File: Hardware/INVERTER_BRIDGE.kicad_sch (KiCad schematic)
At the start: 69 parts, among them Q1 CSD19532Q5B, Q2 CSD19532Q5B, Q3 CSD19532Q5B, Q4 CSD19532Q5B, Q5 CSD19532Q5B, Q6 CSD19532Q5B, U12 UCC27282DRCR, U13 INA240A1PWR, U14 UCC27282DRCR, U15 INA240A1PWR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

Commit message: 拉线，删除电荷泵，修改10Vdcdc斜坡补偿
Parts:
- removed D15, D18, D21: 11V,350mW, Diode_SMD:D_SOD-123, symbol HPM6280Foc:BZT52C11
- removed R27, R32, R37: 10K,1%, Resistor_SMD:R_0402_1005Metric, symbol HPM6280Foc:0402WGF1002TCE

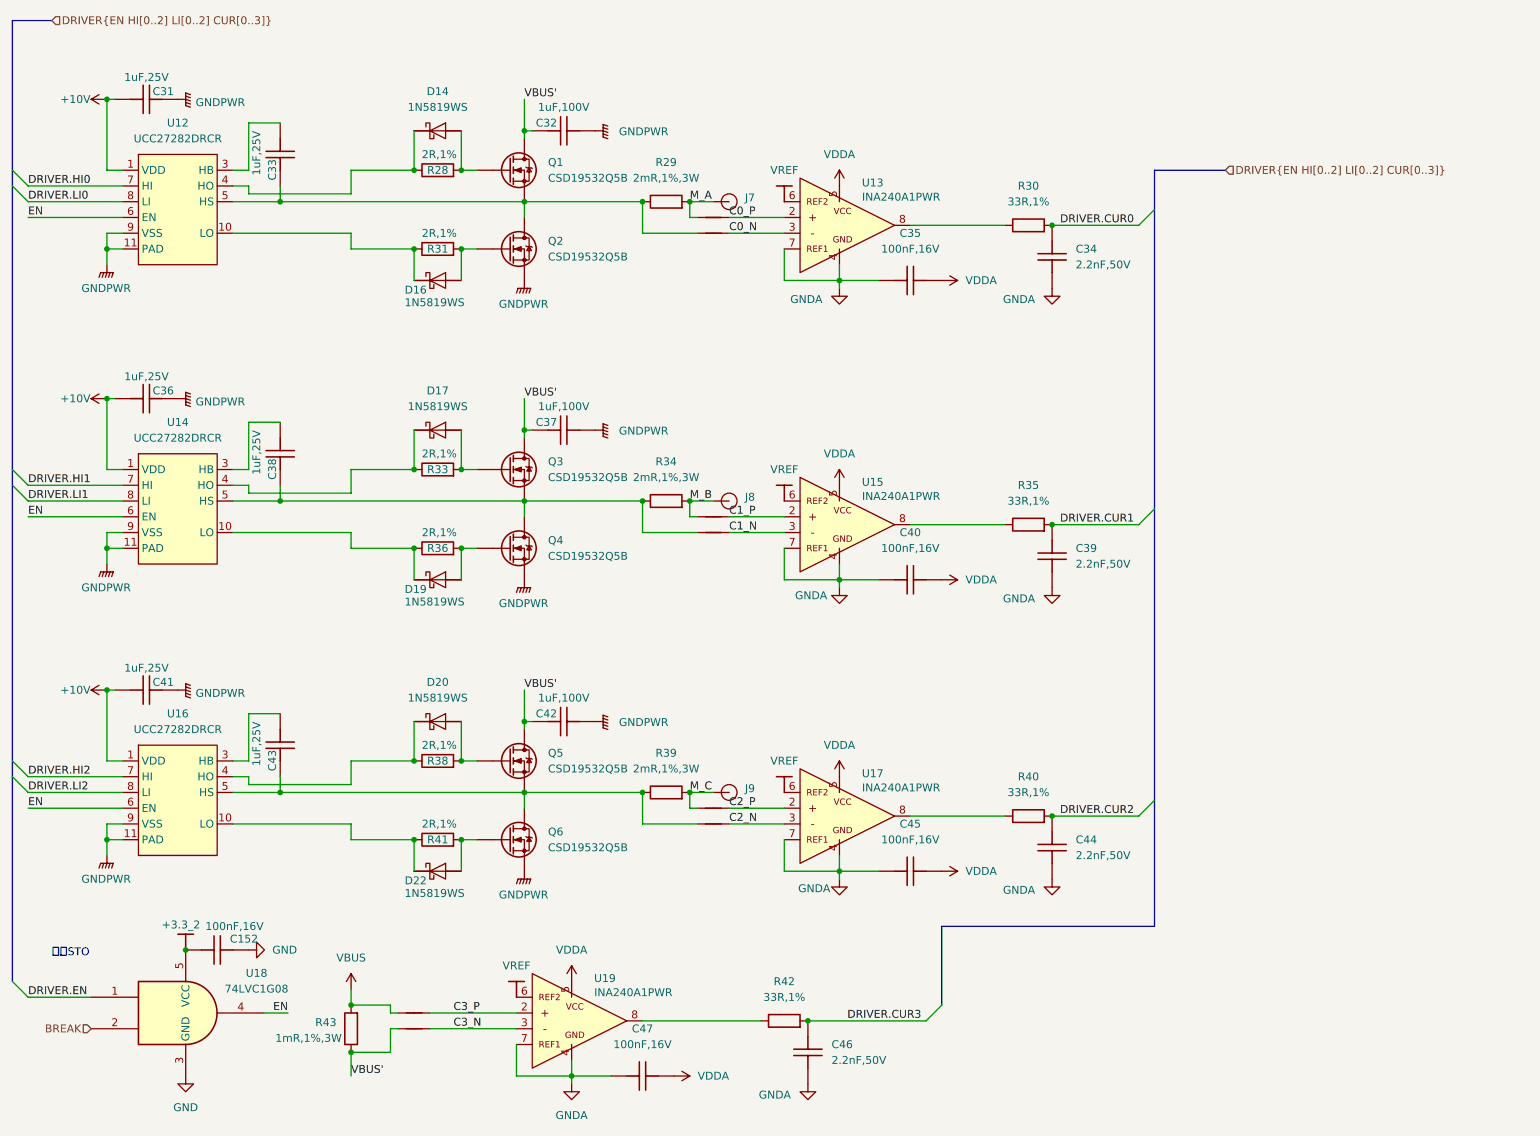
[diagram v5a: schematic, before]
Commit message: PCB和foc_demo
PCB：
部分信号增加测试点
半桥增加栅极电容和RC吸收（待定），泄放mos是否需要栅极电容待测
软件：
增加foc_demo半成品
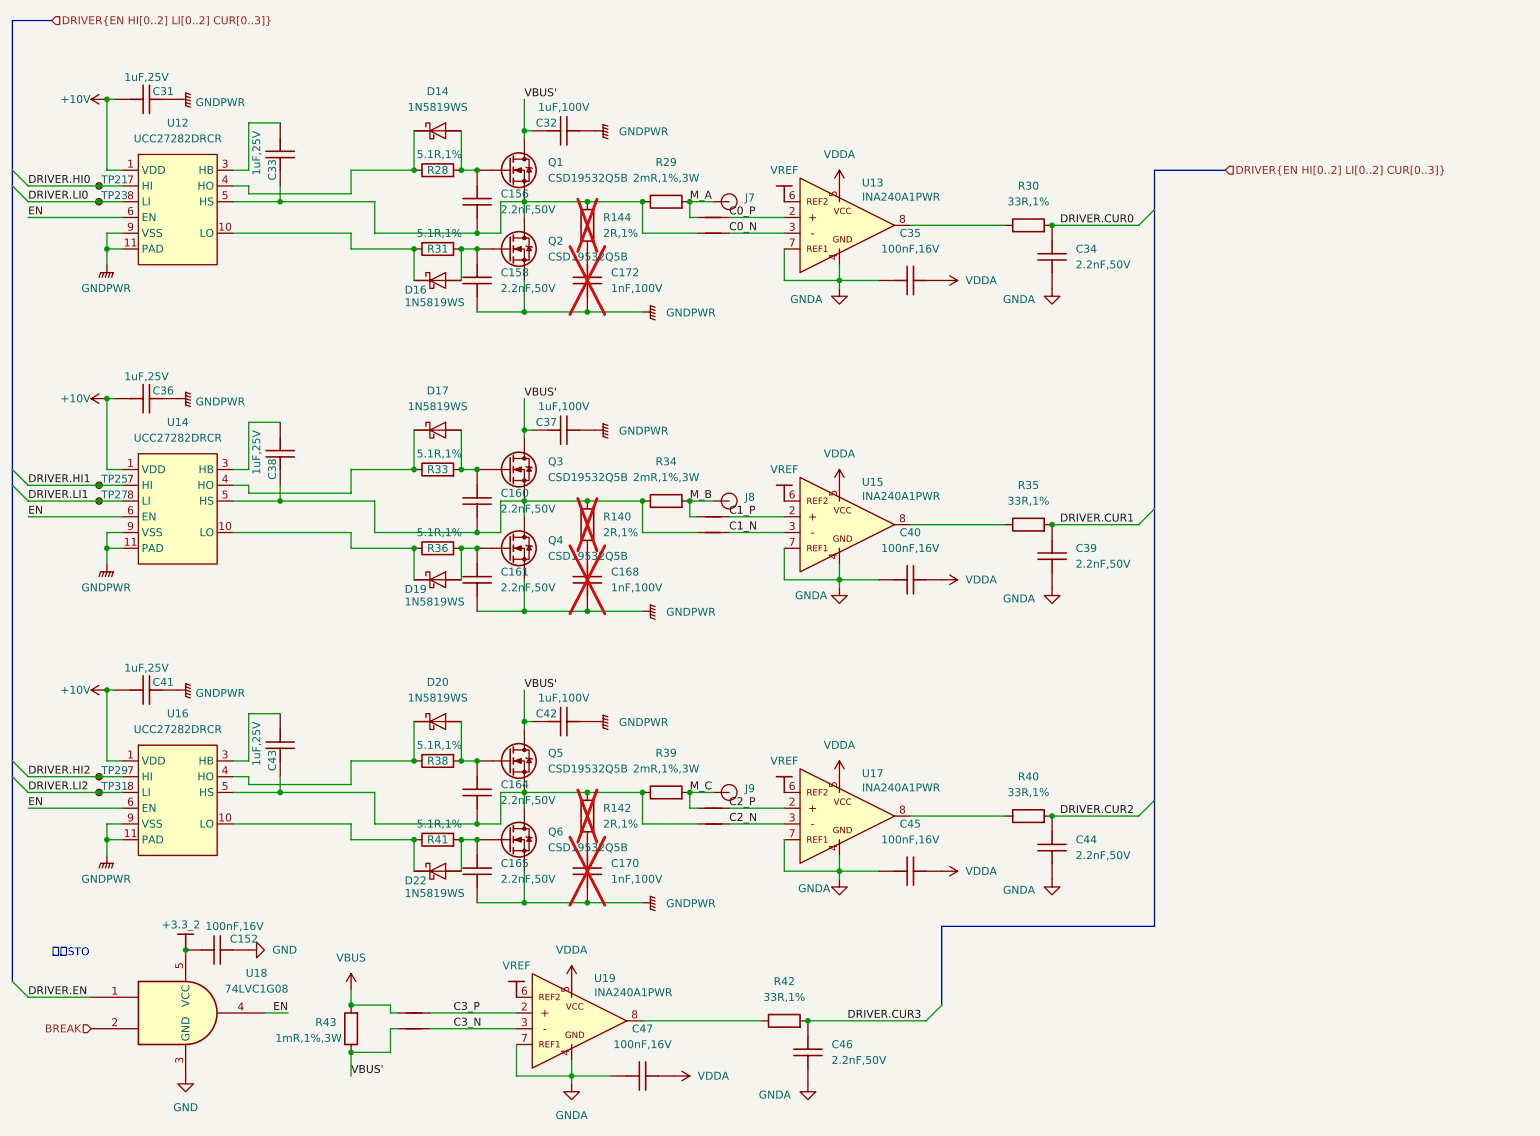
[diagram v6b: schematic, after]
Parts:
- added C156, C158, C160, C161, C164, C165: 2.2nF,50V, Capacitor_SMD:C_0402_1005Metric, symbol HPM6280Foc:0402B222K500NT
- added C168, C170, C172: 1nF,100V, Capacitor_SMD:C_0402_1005Metric, symbol HPM6280Foc:CC0402KRX7R0BB102
- added R140, R142, R144: 2R,1%, Resistor_SMD:R_0402_1005Metric, symbol HPM6280Foc:0402WGF200KTCE
- added TP21, TP23, TP25, TP27, TP29, TP31: ~, Library:test_point_0.5mm, symbol HPM6280Foc:test_point
- R28, R31, R33, R36, R38, R41: value 2R,1% -> 5.1R,1%; symbol HPM6280Foc:0402WGF200KTCE -> HPM6280Foc:0402WGF510KTCE; 立创编号 C270630 -> C25128
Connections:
- net DRIVER.HI0: now also TP21.1
- net DRIVER.HI1: now also TP25.1
- net DRIVER.HI2: now also TP29.1
- net DRIVER.LI0: now also TP23.1
- net DRIVER.LI1: now also TP27.1
- net DRIVER.LI2: now also TP31.1
- net GNDPWR: now also C158.2, C161.2, C165.2, C168.2, C170.2, C172.2
- net at D17.2 (A), Q3.2 (G), R33.2: now also C160.1
- net at C43.2, NT6.1, Q5.3 (S)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: now also C164.2, R142.2
- net at D22.2 (A), Q6.2 (G), R41.2: now also C165.1
- net at D19.2 (A), Q4.2 (G), R36.2: now also C161.1
- net at D14.2 (A), Q1.2 (G), R28.2: now also C156.1
- net at C38.2, NT4.1, Q3.3 (S)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: now also C160.2, R140.2
- net at D20.2 (A), Q5.2 (G), R38.2: now also C164.1
- net at C33.2, NT2.1, Q1.3 (S)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: now also C156.2, R144.2
- net at D16.2 (A), Q2.2 (G), R31.2: now also C158.1
- new net: C168.1, R140.1
- new net: C170.1, R142.1
- new net: C172.1, R144.1

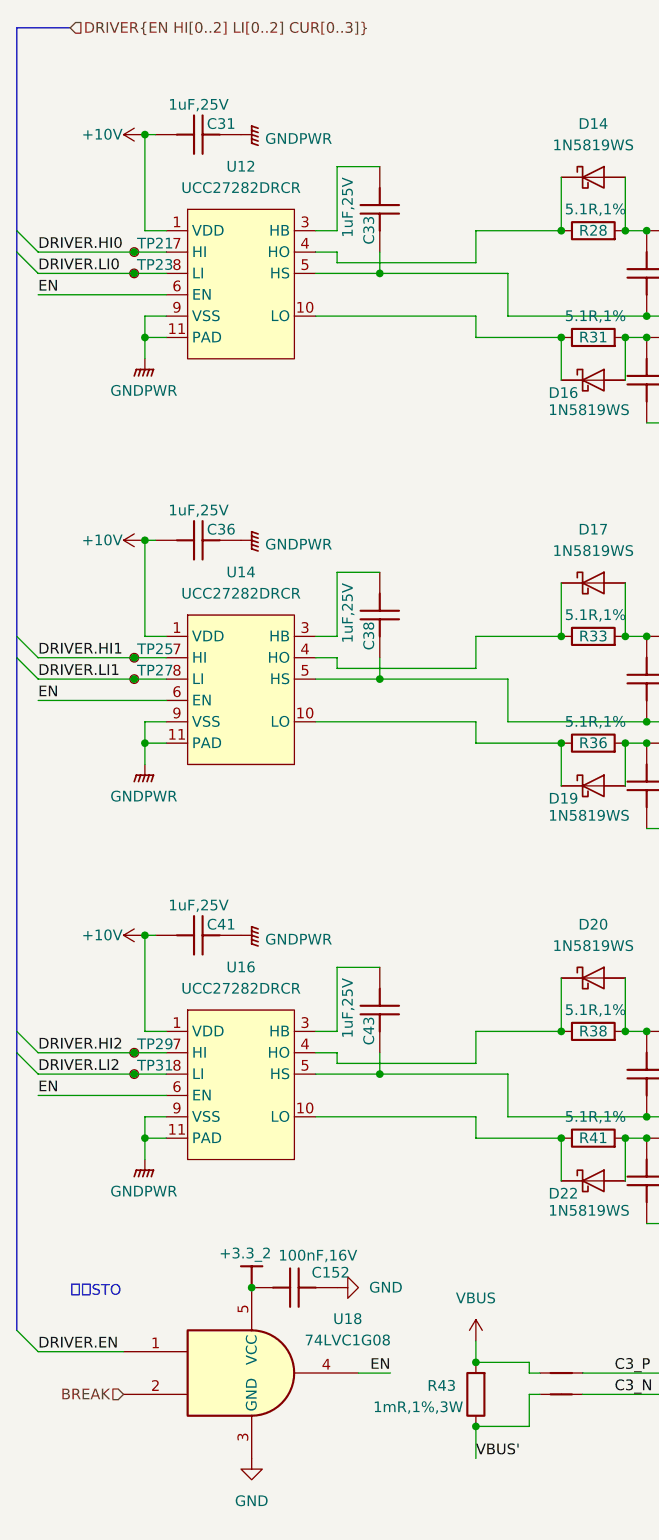
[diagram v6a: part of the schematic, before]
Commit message: PCB优化，修改母线电流采样电阻为2mR，栅极驱动器输入pwm增加滤波防干扰，其他少量优化
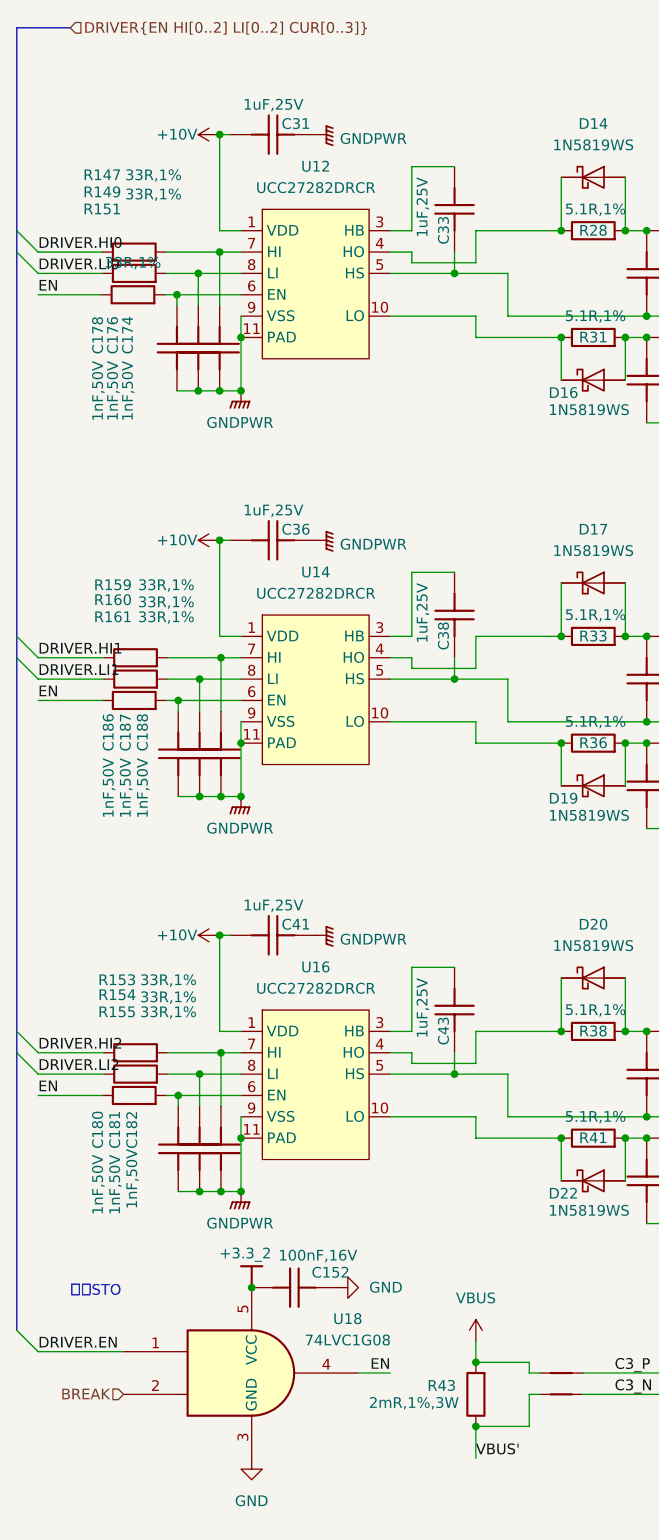
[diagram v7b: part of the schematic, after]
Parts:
- removed TP21, TP23, TP25, TP27, TP29, TP31: ~, Library:test_point_0.5mm, symbol HPM6280Foc:test_point
- added C174, C176, C178, C180, C181, C182, C186, C187, C188: 1nF,50V, Capacitor_SMD:C_0201_0603Metric, symbol HPM6280Foc:CC0201KRX7R9BB102
- added R147, R149, R151, R153, R154, R155, R159, R160, R161: 33R,1%, Resistor_SMD:R_0201_0603Metric, symbol HPM6280Foc:RC0201FR-0733RL
- R43: value 1mR,1%,3W -> 2mR,1%,3W; symbol HPM6280Foc:HoJLR2512-3W-1mR-1% -> HPM6280Foc:HoLLR2512-3W-2mR-1%; 华秋编号 G6676410 -> G11502563; 立创编号 C2903470 -> C2994640
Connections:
- net DRIVER.HI0: now also R147.1; no longer U12.7 (HI)
- net DRIVER.HI1: now also R159.1; no longer U14.7 (HI)
- net DRIVER.HI2: now also R153.1; no longer U16.7 (HI)
- net DRIVER.LI0: now also R149.1; no longer U12.8 (LI)
- net DRIVER.LI1: now also R160.1; no longer U14.8 (LI)
- net DRIVER.LI2: now also R154.1; no longer U16.8 (LI)
- net EN: now also R151.1, R155.1, R161.1; no longer U12.6 (EN), U14.6 (EN), U16.6 (EN)
- net GNDPWR: now also C174.2, C176.2, C178.2, C180.2, C181.2, C182.2, C186.2, C187.2, C188.2
- new net: C181.1, R154.2, U16.8 (LI)
- new net: C188.1, R159.2, U14.7 (HI)
- new net: C187.1, R160.2, U14.8 (LI)
- new net: C182.1, R153.2, U16.7 (HI)
- new net: C174.1, R147.2, U12.7 (HI)
- new net: C176.1, R149.2, U12.8 (LI)
- new net: C186.1, R161.2, U14.6 (EN)
- new net: C180.1, R155.2, U16.6 (EN)
- new net: C178.1, R151.2, U12.6 (EN)
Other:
- moved on the sheet: C31, C33, C36, C38, C41, C43, U12, U14, U16

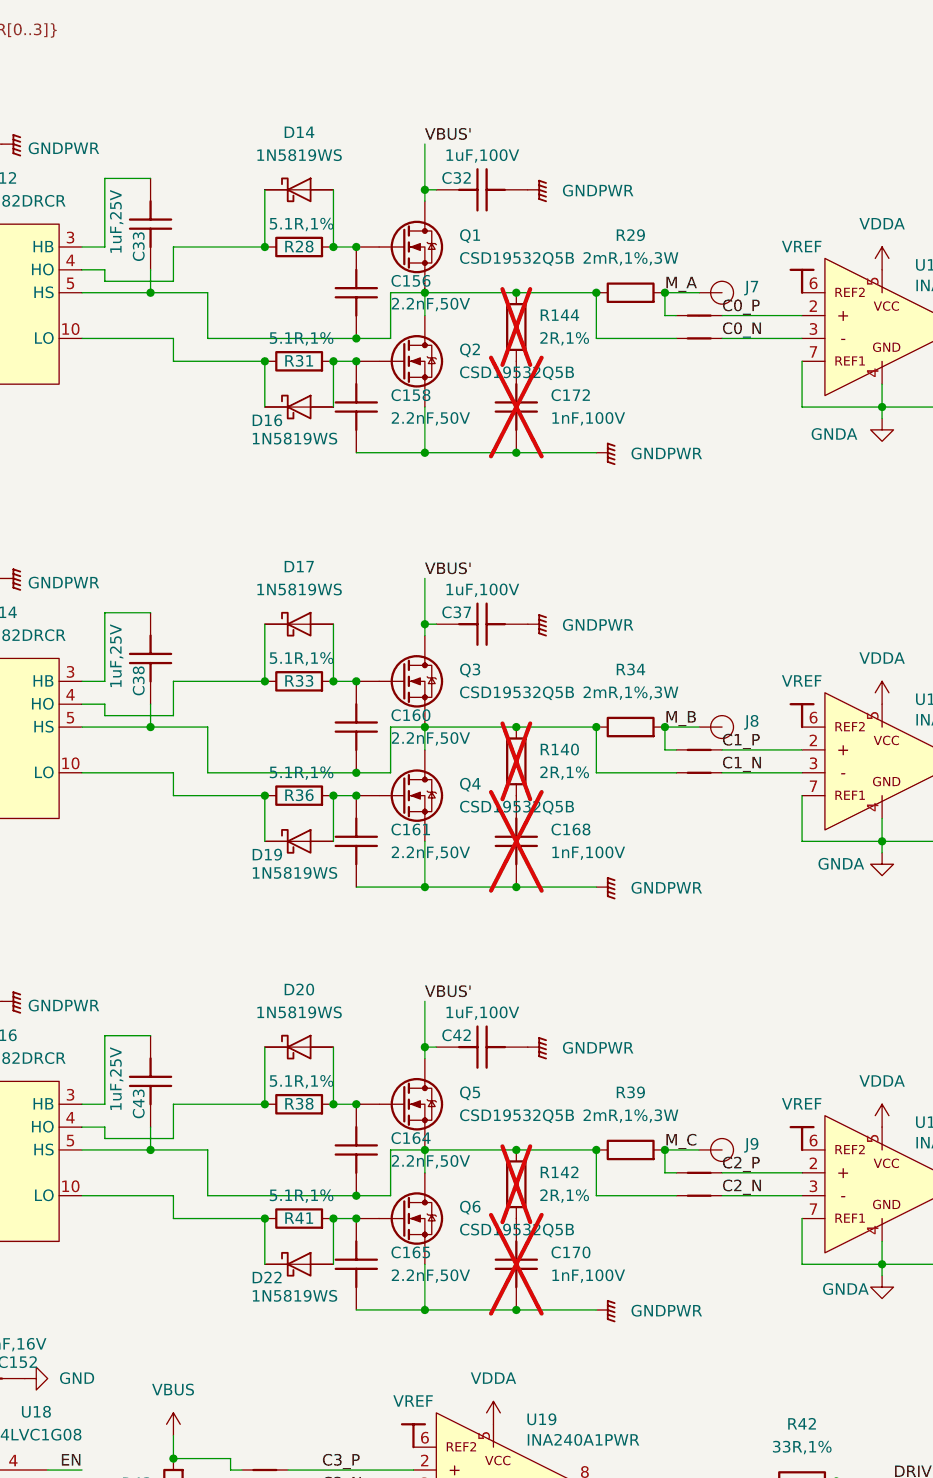
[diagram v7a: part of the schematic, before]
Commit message: PCB修改栅极电阻，增加上侧RC吸收电路，同步修改软件死区时间到150ns
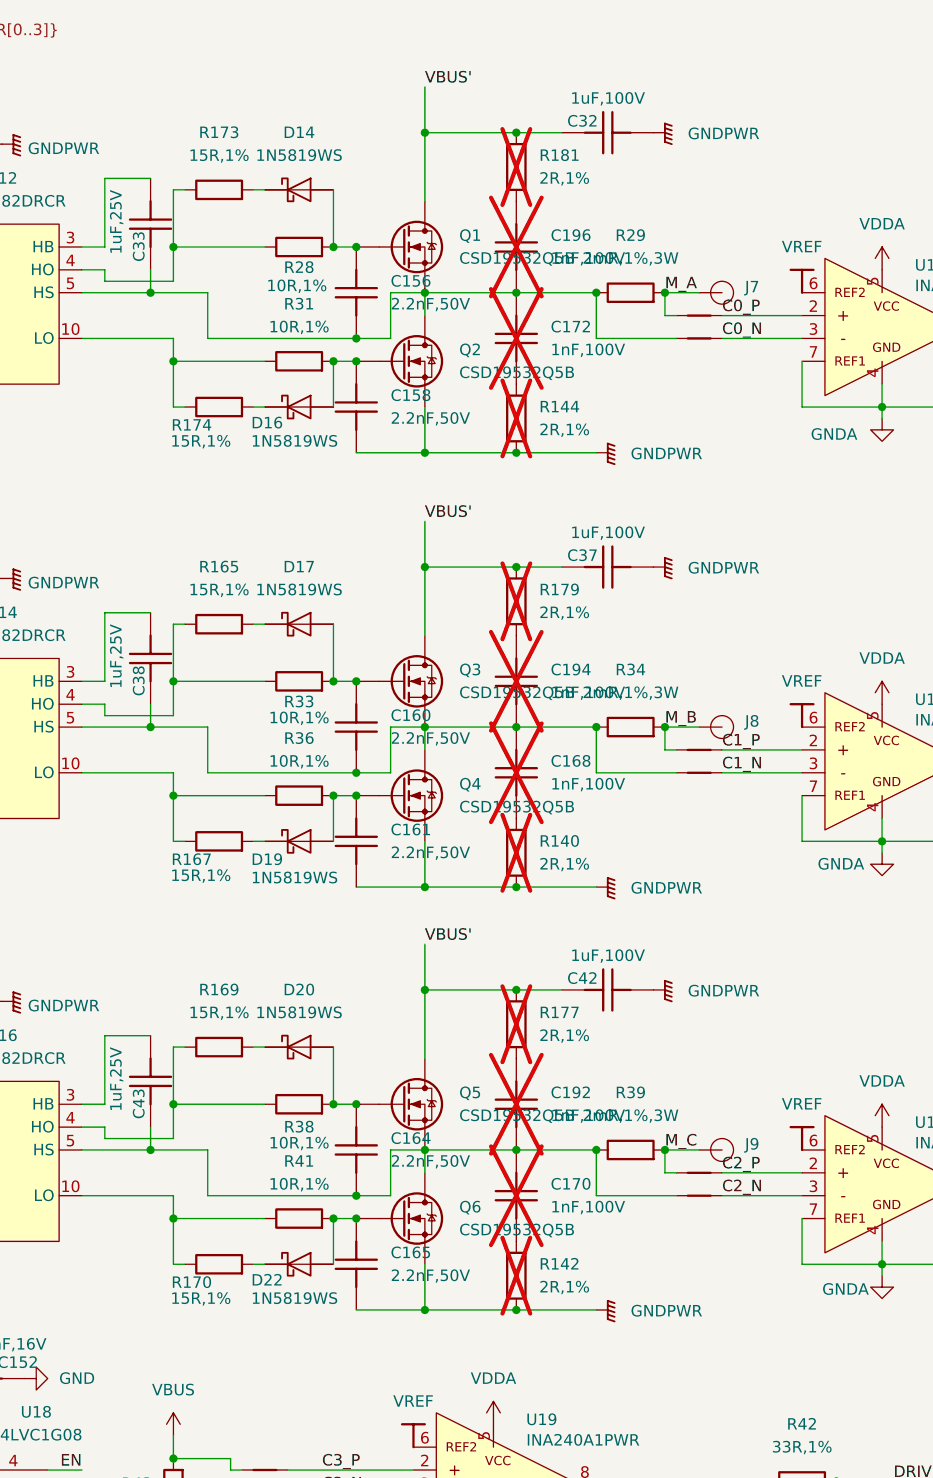
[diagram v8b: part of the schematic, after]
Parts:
- added C192, C194, C196: 1nF,100V, Capacitor_SMD:C_0402_1005Metric, symbol HPM6280Foc:CC0402KRX7R0BB102
- added R165, R167, R169, R170, R173, R174: 15R,1%, Resistor_SMD:R_0402_1005Metric, symbol HPM6280Foc:0402WGF150JTCE
- added R177, R179, R181: 2R,1%, Resistor_SMD:R_0402_1005Metric, symbol HPM6280Foc:0402WGF200KTCE
- R28, R31, R33, R36, R38, R41: value 5.1R,1% -> 10R,1%; symbol HPM6280Foc:0402WGF510KTCE -> HPM6280Foc:0402WGF100JTCE; 制造商 (none) -> UNI-ROYAL(厚声); 华秋编号 G3327760 -> G3704098; 立创编号 C25128 -> C25077
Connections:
- net GNDPWR: now also R140.1, R142.1, R144.1; no longer C168.2, C170.2, C172.2
- net VBUS': now also R177.2, R179.2, R181.2
- net at C156.2, C33.2, NT2.1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: now also C172.1, C196.2; no longer R144.2
- net at R33.1, U14.4 (HO): now also R165.1; no longer D17.1 (K)
- net at C164.2, C43.2, NT6.1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: now also C170.1, C192.2; no longer R142.2
- net at C168.1: now also C160.2, C38.2, NT4.1, Q3.3 (S), Q4.1 (D), R34.1, U14.5 (HS), C194.2; no longer R140.1
- net at R36.1, U14.10 (LO): now also R167.1; no longer D19.1 (K)
- net at R28.1, U12.4 (HO): now also R173.1; no longer D14.1 (K)
- net at R41.1, U16.10 (LO): now also R170.1; no longer D22.1 (K)
- net at R38.1, U16.4 (HO): now also R169.1; no longer D20.1 (K)
- net at R31.1, U12.10 (LO): now also R174.1; no longer D16.1 (K)
- new net: C194.1, R179.1
- new net: D17.1 (K), R165.2
- new net: C196.1, R181.1
- new net: C168.2, R140.2
- new net: D19.1 (K), R167.2
- new net: D14.1 (K), R173.2
- new net: C192.1, R177.1
- new net: D22.1 (K), R170.2
- new net: C170.2, R142.2
- new net: D20.1 (K), R169.2
- new net: C172.2, R144.2
- new net: D16.1 (K), R174.2
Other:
- moved on the sheet: C168, C170, C172, C32, C37, C42, R140, R142, R144
